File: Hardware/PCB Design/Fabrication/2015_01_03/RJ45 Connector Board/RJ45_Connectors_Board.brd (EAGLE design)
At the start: 75.7 x 64.3 mm, 65 parts

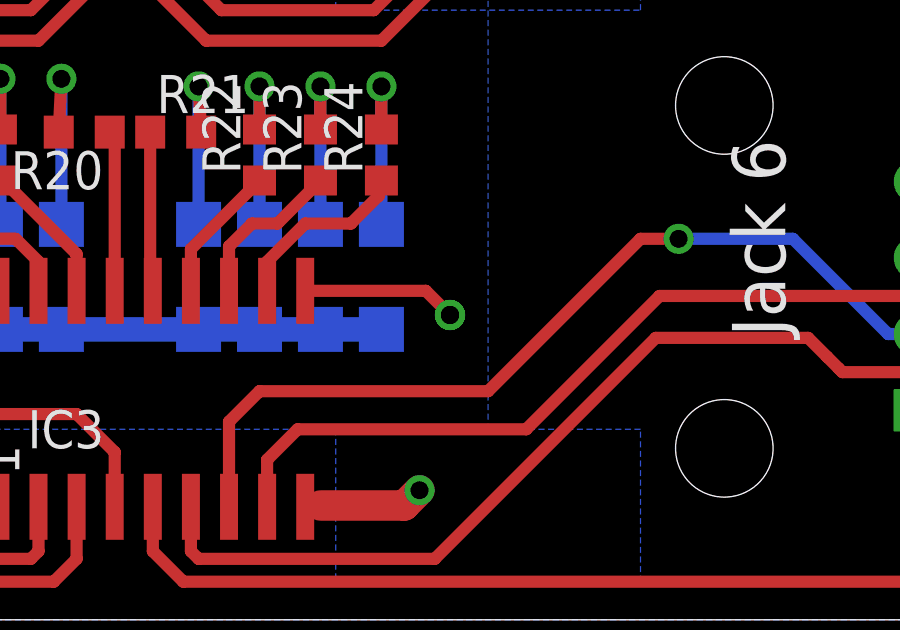
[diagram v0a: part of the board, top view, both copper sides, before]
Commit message: Compiled files needed for PCB fabrication, and assembly,
Also the BOM and the parts number that we are shipping.
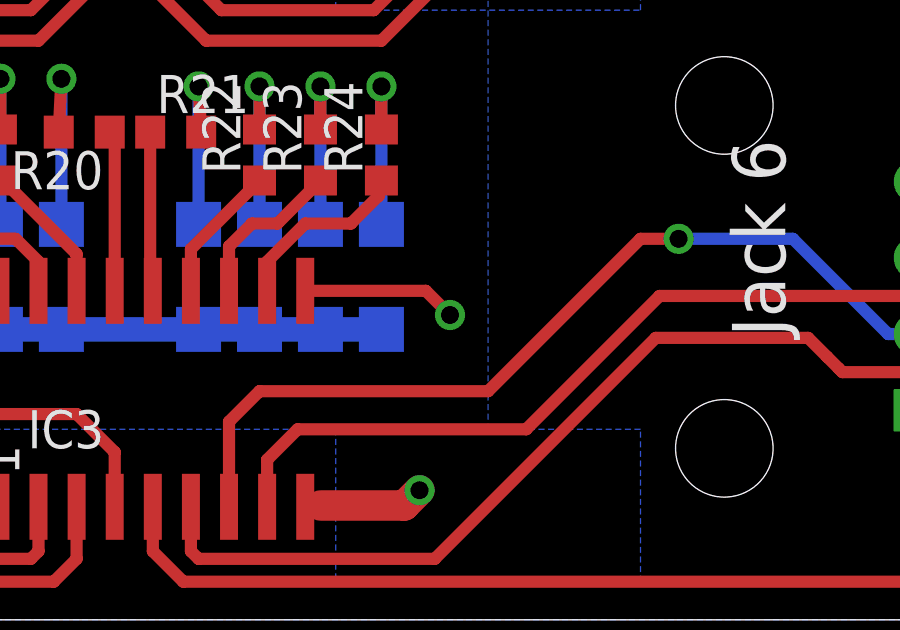
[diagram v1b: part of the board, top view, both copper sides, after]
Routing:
- net +5V: vias 4 -> 3
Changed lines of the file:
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@@
 </polygon>
-<via x="48.26" y="26.67" extent="1-16" drill="0.6"/>
 <via x="48.26" y="26.67" extent="1-16" drill="0.6"/>
 <via x="48.26" y="46.99" extent="1-16" drill="0.6"/>
